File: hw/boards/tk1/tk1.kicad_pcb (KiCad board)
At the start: 4 copper layers, 27.5 x 13.5 mm, 68 parts, among them P1 USB_C_Plug, U1 MCP1824T-2502EOT, U10 PT2043AT6, U2 MIC5258-1.2YM5, U3 CH552E, U5 USBLC6-2SC6, U6 ICE40UP5K-SG48ITR, U8 XT25F08BDFIGT-S, U9 NCP752BSN33T1G

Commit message: TK-1 release
* Add dimensions for PCB
* Add layer stackup for PCB
* Change PCB component origin to match expanded board
* Change schematic title to 'TK-1', update release date
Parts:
- C27: value 10pF -> 1pF
- C8: value 10uF -> 1uF
- TP1, TP12, TP13, TP14, TP15, TP16, TP17, TP18, TP19, TP2, TP20, TP21, TP28, TP3, TP4, TP5, TP6, TP7, TP8, TP9: footprint TestPoint:TestPoint_Pad_D1.0mm -> mta1:TestPoint_Pad_D1.0mm
- U8: value XT25F08BDFIGT-S -> W25Q80DVUXIE
- turned TP1 to 0 degrees
- turned TP2 to 180 degrees
- turned TP3 to 0 degrees
- turned TP4 to 0 degrees
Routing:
- net GND: track 38.0 -> 39.6 mm, vias 38 -> 37
- net APP_ICE_MISO: track 9.88 -> 8.46 mm
- net +3V3: track 36.7 -> 37.8 mm
- net INTERFACE_RX: track 10.1 -> 11.0 mm
- net INTERFACE_CTS: track 8.98 -> 8.38 mm
- net +2V5: track 17.3 -> 17.8 mm
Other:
- board size 27.5 x 13.5 mm -> 27.7 x 13.9 mm
- board text added: "0"
- board text added: "0 mm"
- board text added: "0.01 mm"
- board text added: "0.0175 mm"
- board text added: "0.02"
- board text added: "0.035 mm"
- board text added: "0.121 mm"
- board text added: "0.433 mm"
- board text added: "1"
- board text added: "2022-11 RevA"
- board text added: "3.3"
- board text added: "4.5"
- board text added: "B.Cu"
- board text added: "B.Mask"
- board text added: "B.Paste"
- board text added: "B.Silkscreen"
- board text added: "Black"
- board text added: "Bottom Silk Screen"
- board text added: "Bottom Solder Mask"
- board text added: "Bottom Solder Paste"
- board text added: "Color"
- board text added: "Dielectric 1"
- board text added: "Dielectric 2"
- board text added: "Dielectric 3"
- board text added: "Epsilon R"
- board text added: "F.Cu"
- board text added: "F.Mask"
- board text added: "F.Paste"
- board text added: "F.Silkscreen"
- board text added: "FR4"
- board text added: "In1.Cu"
- board text added: "In2.Cu"
- board text added: "Layer Name"
- board text added: "Loss Tangent"
- board text added: "Material"
- board text added: "Not specified"
- board text added: "Thickness (mm)"
- board text added: "Tillitis TK-1"
- board text added: "Top Silk Screen"
- board text added: "Top Solder Mask"
- board text added: "Top Solder Paste"
- board text added: "Type"
- board text added: "White"
- board text added: "copper"
- board text added: "core"
- board text added: "prepreg"
- board text removed: "+1.2V"
- board text removed: "+2.5V"
- board text removed: "+3.3V"
- board text removed: "+5V"
- board text removed: "Test pads on bottom:"
- board text removed: "Tillitis TK1"

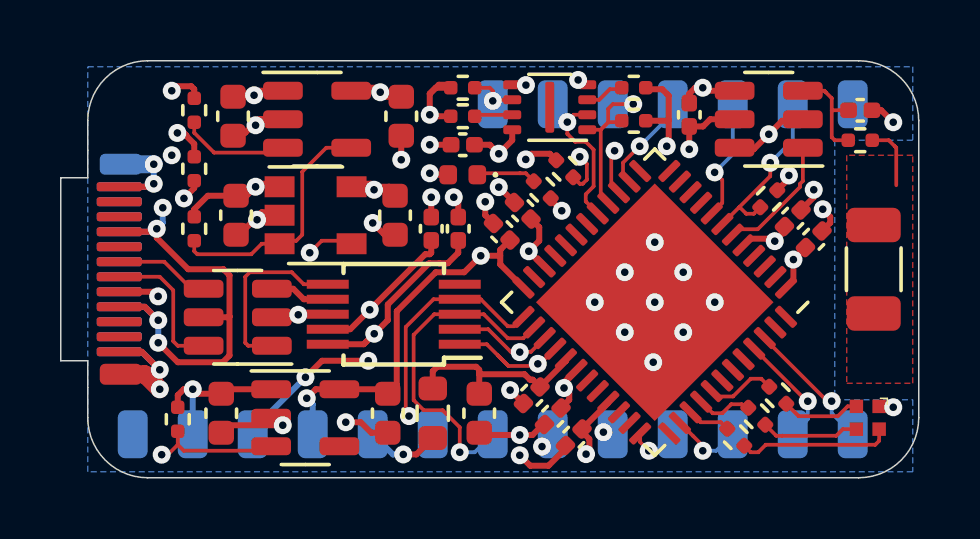
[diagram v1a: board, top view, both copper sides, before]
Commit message: TK-1: RevA.1 release
* Add two fiducials to TK-1 board
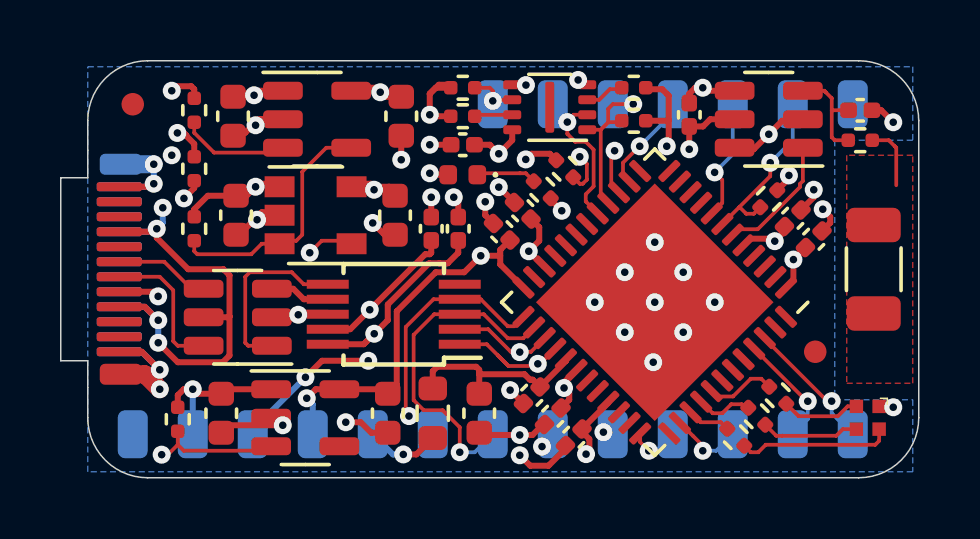
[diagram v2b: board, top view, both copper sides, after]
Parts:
- added FID1: Fiducial, Fiducial:Fiducial_0.75mm_Mask1.5mm, F.Cu at (101.5, 88.5)
- added FID2: Fiducial, Fiducial:Fiducial_0.75mm_Mask1.5mm, F.Cu at (124.2, 96.8)
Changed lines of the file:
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@@
     )
+  )
+  (footprint "Fiducial:Fiducial_0.75mm_Mask1.5mm" (layer "F.Cu")
+    (at 101.5 88.5)
+    (descr "Circular Fiducial, 0.75mm bare copper, 1.5mm soldermask opening (Level B)")
+    (tags "fiducial")
+    (property "Sheetfile" "tk1.kicad_sch")
+    (property "Sheetname" "")
+    (property "exclude_from_bom" "")
+    (attr smd exclude_from_bom)
+    (fp_text reference "FID1" (at 0 -2) (layer "F.SilkS") hide
+      (effects (font (size 1 1) (thickness 0.15)))
+    )
+    (fp_text value "Fiducial" (at 0 2) (layer "F.Fab")
+      (effects (font (size 1 1) (thickness 0.15)))
+    )
+    (fp_text user "${REFERENCE}" (at 0 0) (layer "F.Fab")
+      (effects (font (size 0.3 0.3) (thickness 0.05)))
+    )
+    (fp_circle (center 0 0) (end 1 0) (layer "F.CrtYd") (width 0.05) (fill none))
+    (fp_circle (center 0 0) (end 0.75 0) (layer "F.Fab") (width 0.1) (fill none))
+    (pad "" smd circle (at 0 0) (size 0.75 0.75) (layers "F.Cu" "F.Mask")
+      (solder_mask_margin 0.375) (clearance 0.375))
+  )
+  (footprint "Fiducial:Fiducial_0.75mm_Mask1.5mm" (layer "F.Cu")
+    (at 124.25 96.75)
+    (descr "Circular Fiducial, 0.75mm bare copper, 1.5mm soldermask opening (Level B)")
+    (tags "fiducial")
+    (property "Sheetfile" "tk1.kicad_sch")
+    (property "Sheetname" "")
+    (property "exclude_from_bom" "")
+    (attr smd exclude_from_bom)
+    (fp_text reference "FID2" (at 0 -2) (layer "F.SilkS") hide
+      (effects (font (size 1 1) (thickness 0.15)))
+    )
+    (fp_text value "Fiducial" (at 0 2) (layer "F.Fab")
+      (effects (font (size 1 1) (thickness 0.15)))
+    )
+    (fp_text user "${REFERENCE}" (at 0 0) (layer "F.Fab")
+      (effects (font (size 0.3 0.3) (thickness 0.05)))
+    )
+    (fp_circle (center 0 0) (end 1 0) (layer "F.CrtYd") (width 0.05) (fill none))
+    (fp_circle (center 0 0) (end 0.75 0) (layer "F.Fab") (width 0.1) (fill none))
+    (pad "" smd circle (at 0 0) (size 0.75 0.75) (layers "F.Cu" "F.Mask")
+      (solder_mask_margin 0.375) (clearance 0.375))
   )
   (footprint "mta1:CAPC1005X06L" (layer "F.Cu")
